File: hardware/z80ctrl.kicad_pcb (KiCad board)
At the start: 2 copper layers, 99.8 x 49.9 mm, 28 parts, among them J1 BUS, J2 BUSEXT, J4 IOADDR, J5 SERIAL1, J6 SERIAL2, J7 SD, SW1 RESET, SW2 HALT, U1 74HCT139, U2 ATMEGA1284P-PU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

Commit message: OCD tweaks
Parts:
- moved C3 0.25 mm to (239.3, 145.0)
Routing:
- net /SDCS: track 104.2 -> 102.1 mm

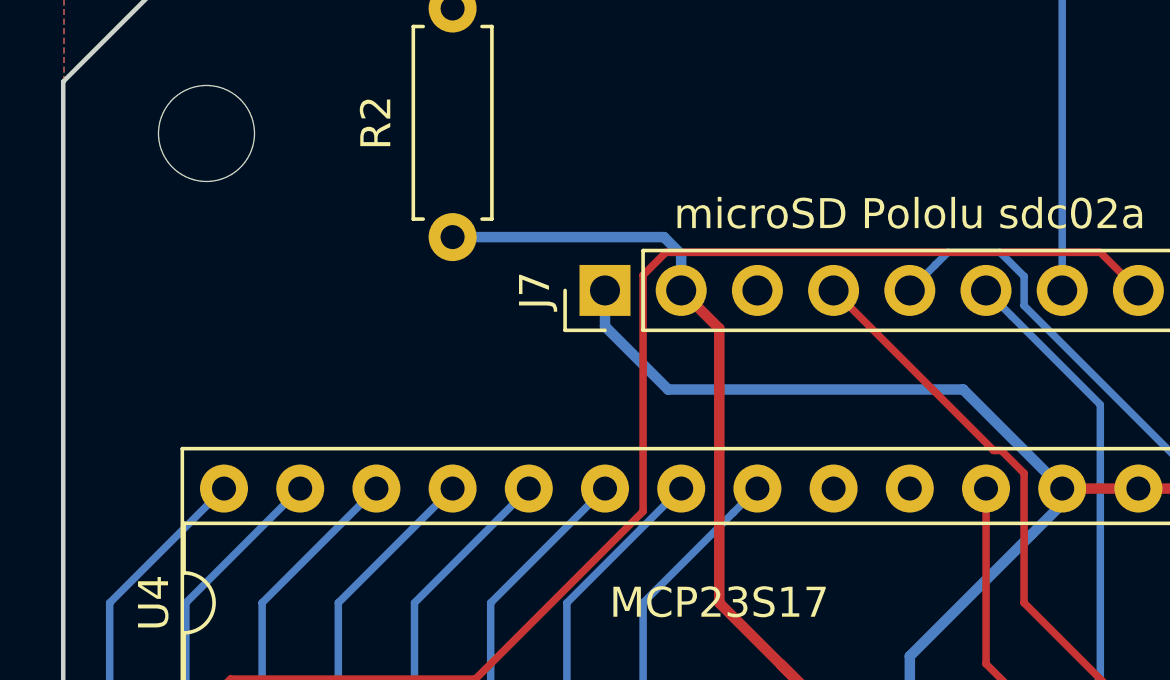
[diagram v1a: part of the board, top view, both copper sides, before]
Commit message: Add ISP header to REV2
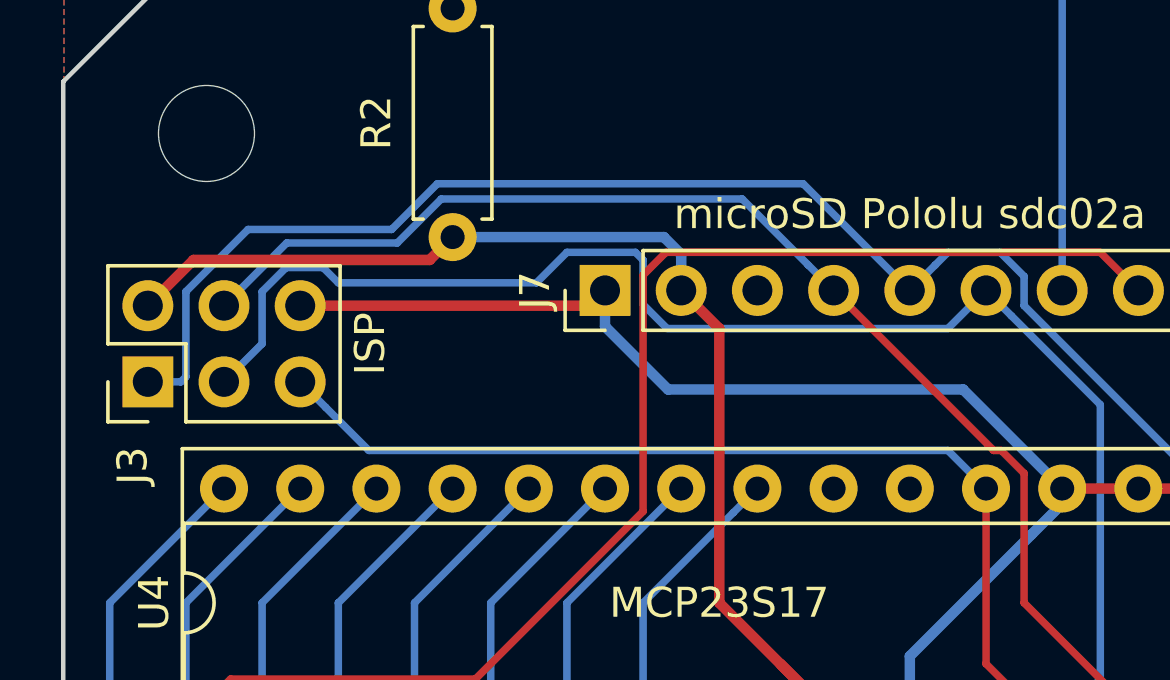
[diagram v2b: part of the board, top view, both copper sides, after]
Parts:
- added J3: ISP, Pin_Headers:Pin_Header_Straight_2x03_Pitch2.54mm, F.Cu at (157.0, 128.5)
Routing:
- net MISO: track 96.5 -> 127.8 mm
- net SCK: track 95.8 -> 126.9 mm
- net /AVRRST: track 129.7 -> 154.1 mm
- net MOSI: track 98.1 -> 121.1 mm
- net VCC: track 207.1 -> 218.2 mm
- net GND: track 308.0 -> 318.4 mm
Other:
- board text added: "z80ctrl REV2 (C)2018 J.B. Langston https://github.com/jblang/z80ctrl"
- board text removed: "(C)2018 J.B. Langston https://github.com/jblang/z80ctrl"
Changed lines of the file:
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@@
 (kicad_pcb (version 4) (host pcbnew 4.0.7)
   (general
-    (links 142)
+    (links 148)
     (no_connects 0)
-    (area 153.676999 46.9809 262.997001 153.663001)
+    (area 154.077599 103.429999 254.027601 153.440201)
     (thickness 1.6)
     (drawings 15)
-    (tracks 712)
+    (tracks 748)
     (zones 0)
-    (modules 28)
+    (modules 29)
     (nets 90)
   )
@@
     )
   )
+  (module Pin_Headers:Pin_Header_Straight_2x03_Pitch2.54mm (layer F.Cu)
+    (at 156.972 128.524 90)
+    (descr "Through hole straight pin header, 2x03, 2.54mm pitch, double rows")
+    (tags "Through hole pin header THT 2x03 2.54mm double row")
+    (fp_text reference J3 (at -2.794 -0.508 90) (layer F.SilkS)
+      (effects (font (size 1 1) (thickness 0.15)))
+    )
+    (fp_text value ISP (at 1.27 7.41 90) (layer F.SilkS)
+      (effects (font (size 1 1) (thickness 0.15)))
+    )
+    (fp_line (start 0 -1.27) (end 3.81 -1.27) (layer F.Fab) (width 0.1))
+    (fp_line (start 3.81 -1.27) (end 3.81 6.35) (layer F.Fab) (width 0.1))
+    (fp_line (start 3.81 6.35) (end -1.27 6.35) (layer F.Fab) (width 0.1))
+    (fp_line (start -1.27 6.35) (end -1.27 0) (layer F.Fab) (width 0.1))
+    (fp_line (start -1.27 0) (end 0 -1.27) (layer F.Fab) (width 0.1))
+    (fp_line (start -1.33 6.41) (end 3.87 6.41) (layer F.SilkS) (width 0.12))
+    (fp_line (start -1.33 1.27) (end -1.33 6.41) (layer F.SilkS) (width 0.12))
+    (fp_line (start 3.87 -1.33) (end 3.87 6.41) (layer F.SilkS) (width 0.12))
+    (fp_line (start -1.33 1.27) (end 1.27 1.27) (layer F.SilkS) (width 0.12))
+    (fp_line (start 1.27 1.27) (end 1.27 -1.33) (layer F.SilkS) (width 0.12))
+    (fp_line (start 1.27 -1.33) (end 3.87 -1.33) (layer F.SilkS) (width 0.12))
+    (fp_line (start -1.33 0) (end -1.33 -1.33) (layer F.SilkS) (width 0.12))
+    (fp_line (start -1.33 -1.33) (end 0 -1.33) (layer F.SilkS) (width 0.12))
+    (fp_line (start -1.8 -1.8) (end -1.8 6.85) (layer F.CrtYd) (width 0.05))
+    (fp_line (start -1.8 6.85) (end 4.35 6.85) (layer F.CrtYd) (width 0.05))
+    (fp_line (start 4.35 6.85) (end 4.35 -1.8) (layer F.CrtYd) (width 0.05))
+    (fp_line (start 4.35 -1.8) (end -1.8 -1.8) (layer F.CrtYd) (width 0.05))
+    (fp_text user %R (at 1.27 2.54 180) (layer F.Fab)
+      (effects (font (size 1 1) (thickness 0.15)))
+    )
+    (pad 1 thru_hole rect (at 0 0 90) (size 1.7 1.7) (drill 1) (layers *.Cu *.Mask)
+      (net 48 MISO))
+    (pad 2 thru_hole oval (at 2.54 0 90) (size 1.7 1.7) (drill 1) (layers *.Cu *.Mask)
+      (net 2 VCC))
+    (pad 3 thru_hole oval (at 0 2.54 90) (size 1.7 1.7) (drill 1) (layers *.Cu *.Mask)
+      (net 47 SCK))
+    (pad 4 thru_hole oval (at 2.54 2.54 90) (size 1.7 1.7) (drill 1) (layers *.Cu *.Mask)
+      (net 49 MOSI))
+    (pad 5 thru_hole oval (at 0 5.08 90) (size 1.7 1.7) (drill 1) (layers *.Cu *.Mask)
+      (net 43 /AVRRST))
+    (pad 6 thru_hole oval (at 2.54 5.08 90) (size 1.7 1.7) (drill 1) (layers *.Cu *.Mask)
+      (net 1 GND))
+    (model ${KISYS3DMOD}/Pin_Headers.3dshapes/Pin_Header_Straight_2x03_Pitch2.54mm.wrl
+      (at (xyz 0 0 0))
+      (scale (xyz 1 1 1))
+      (rotate (xyz 0 0 0))
+    )
+  )
   (gr_text "microSD Pololu sdc02a" (at 182.372 122.936) (layer F.SilkS)
     (effects (font (size 1 1) (thickness 0.15)))
@@
     (effects (font (size 1 1) (thickness 0.15)) (justify left mirror))
   )
-  (gr_text "(C)2018 J.B. Langston\nhttps://github.com/jblang/z80ctrl" (at 223.52 132.588) (layer B.SilkS)
+  (gr_text "z80ctrl REV2\n(C)2018 J.B. Langston\nhttps://github.com/jblang/z80ctrl" (at 223.52 132.08) (layer B.SilkS)
     (effects (font (size 1.5 1.5) (thickness 0.3)) (justify mirror))
   )
@@
   (gr_line (start 154.1526 118.5164) (end 154.1526 153.3652) (angle 90) (layer Edge.Cuts) (width 0.15))
   (gr_line (start 154.1526 153.3652) (end 253.9526 153.3652) (angle 90) (layer Edge.Cuts) (width 0.15))
+  (segment (start 162.052 125.984) (end 171.704 125.984) (width 0.35) (layer F.Cu) (net 1))
+  (segment (start 171.704 125.984) (end 172.212 125.476) (width 0.35) (layer F.Cu) (net 1))
   (segment (start 221.782 145.034) (end 223.56 146.812) (width 0.35) (layer F.Cu) (net 1))
   (segment (start 223.56 146.812) (end 239.99 146.812) (width 0.35) (layer F.Cu) (net 1))
@@
   (segment (start 224.282 142.24) (end 221.782 144.74) (width 0.35) (layer F.Cu) (net 1))
   (segment (start 221.782 144.74) (end 221.782 145.034) (width 0.35) (layer F.Cu) (net 1))
+  (segment (start 156.972 125.984) (end 158.496 124.46) (width 0.35) (layer F.Cu) (net 2))
+  (segment (start 166.37 124.46) (end 167.132 123.698) (width 0.35) (layer F.Cu) (net 2))
+  (segment (start 158.496 124.46) (end 166.37 124.46) (width 0.35) (layer F.Cu) (net 2))
   (segment (start 224.282 124.46) (end 225.806 122.936) (width 0.35) (layer F.Cu) (net 2))
   (segment (start 225.806 122.936) (end 227.33 122.936) (width 0.35) (layer F.Cu) (net 2))
@@
   (segment (start 228.6 145.034) (end 229.362 144.272) (width 0.25) (layer F.Cu) (net 42))
   (segment (start 229.362 142.24) (end 226.822 139.7) (width 0.25) (layer F.Cu) (net 42))
+  (segment (start 184.912 132.08) (end 183.642 130.81) (width 0.25) (layer B.Cu) (net 43))
+  (segment (start 183.642 130.81) (end 164.338 130.81) (width 0.25) (layer B.Cu) (net 43))
+  (segment (start 164.338 130.81) (end 162.901999 129.373999) (width 0.25) (layer B.Cu) (net 43))
+  (segment (start 162.901999 129.373999) (end 162.052 128.524) (width 0.25) (layer B.Cu) (net 43))
   (segment (start 242.062 109.982) (end 249.682 109.982) (width 0.25) (layer F.Cu) (net 43))
   (segment (start 249.682 109.982) (end 250.19 109.982) (width 0.25) (layer B.Cu) (net 43))
@@
   (segment (start 229.577002 109.474) (end 230.632 108.419002) (width 0.25) (layer B.Cu) (net 46))
   (segment (start 230.632 104.648) (end 230.124 104.14) (width 0.25) (layer B.Cu) (net 46))
+  (segment (start 159.512 128.524) (end 160.782 127.254) (width 0.25) (layer B.Cu) (net 47))
+  (segment (start 162.814 124.714) (end 163.322 125.222) (width 0.25) (layer B.Cu) (net 47))
+  (segment (start 163.322 125.222) (end 169.926 125.222) (width 0.25) (layer B.Cu) (net 47))
+  (segment (start 160.782 127.254) (end 160.782 125.514998) (width 0.25) (layer B.Cu) (net 47))
+  (segment (start 183.642 126.746) (end 184.912 125.476) (width 0.25) (layer B.Cu) (net 47))
+  (segment (start 160.782 125.514998) (end 161.582998 124.714) (width 0.25) (layer B.Cu) (net 47))
+  (segment (start 170.942 124.206) (end 173.227002 124.206) (width 0.25) (layer B.Cu) (net 47))
+  (segment (start 161.582998 124.714) (end 162.814 124.714) (width 0.25) (layer B.Cu) (net 47))
+  (segment (start 169.926 125.222) (end 170.942 124.206) (width 0.25) (layer B.Cu) (net 47))
+  (segment (start 173.227002 124.206) (end 173.482 124.460998) (width 0.25) (layer B.Cu) (net 47))
+  (segment (start 173.482 124.460998) (end 173.482 125.945002) (width 0.25) (layer B.Cu) (net 47))
+  (segment (start 173.482 125.945002) (end 174.282998 126.746) (width 0.25) (layer B.Cu) (net 47))
+  (segment (start 174.282998 126.746) (end 183.642 126.746) (width 0.25) (layer B.Cu) (net 47))
   (segment (start 247.991999 150.788001) (end 247.142 151.638) (width 0.25) (layer F.Cu) (net 47))
   (segment (start 248.412 150.368) (end 247.991999 150.788001) (width 0.25) (layer F.Cu) (net 47))
@@
   (segment (start 216.662 139.7) (end 213.925989 142.436011) (width 0.25) (layer F.Cu) (net 47))
   (segment (start 188.251999 140.499999) (end 187.452 139.7) (width 0.25) (layer F.Cu) (net 47))
+  (segment (start 160.312998 123.444) (end 158.242 125.514998) (width 0.25) (layer B.Cu) (net 48))
+  (segment (start 158.242 125.514998) (end 158.242 128.354) (width 0.25) (layer B.Cu) (net 48))
+  (segment (start 182.372 125.476) (end 178.816 121.92) (width 0.25) (layer B.Cu) (net 48))
+  (segment (start 178.816 121.92) (end 166.624 121.92) (width 0.25) (layer B.Cu) (net 48))
+  (segment (start 166.624 121.92) (end 165.1 123.444) (width 0.25) (layer B.Cu) (net 48))
+  (segment (start 165.1 123.444) (end 160.312998 123.444) (width 0.25) (layer B.Cu) (net 48))
+  (segment (start 158.242 128.354) (end 158.072 128.524) (width 0.25) (layer B.Cu) (net 48))
+  (segment (start 158.072 128.524) (end 156.972 128.524) (width 0.25) (layer B.Cu) (net 48))
   (segment (start 250.952 147.19441) (end 250.952 150.368) (width 0.25) (layer F.Cu) (net 48))
   (segment (start 217.227989 136.594011) (end 246.447601 136.594011) (width 0.25) (layer F.Cu) (net 48))
@@
   (segment (start 193.331999 140.499999) (end 192.532 139.7) (width 0.25) (layer F.Cu) (net 48))
   (segment (start 211.836 141.986) (end 194.818 141.986) (width 0.25) (layer F.Cu) (net 48))
+  (segment (start 178.982001 124.626001) (end 179.832 125.476) (width 0.25) (layer B.Cu) (net 49))
+  (segment (start 166.75241 122.428) (end 176.784 122.428) (width 0.25) (layer B.Cu) (net 49))
+  (segment (start 159.512 125.984) (end 161.601989 123.894011) (width 0.25) (layer B.Cu) (net 49))
+  (segment (start 165.2864 123.894011) (end 166.75241 122.428) (width 0.25) (layer B.Cu) (net 49))
+  (segment (start 176.784 122.428) (end 178.982001 124.626001) (width 0.25) (layer B.Cu) (net 49))
+  (segment (start 161.601989 123.894011) (end 165.2864 123.894011) (width 0.25) (layer B.Cu) (net 49))
   (segment (start 212.381999 138.900001) (end 211.582 139.7) (width 0.25) (layer F.Cu) (net 49))
   (segment (start 246.634 136.144) (end 215.138 136.144) (width 0.25) (layer F.Cu) (net 49))

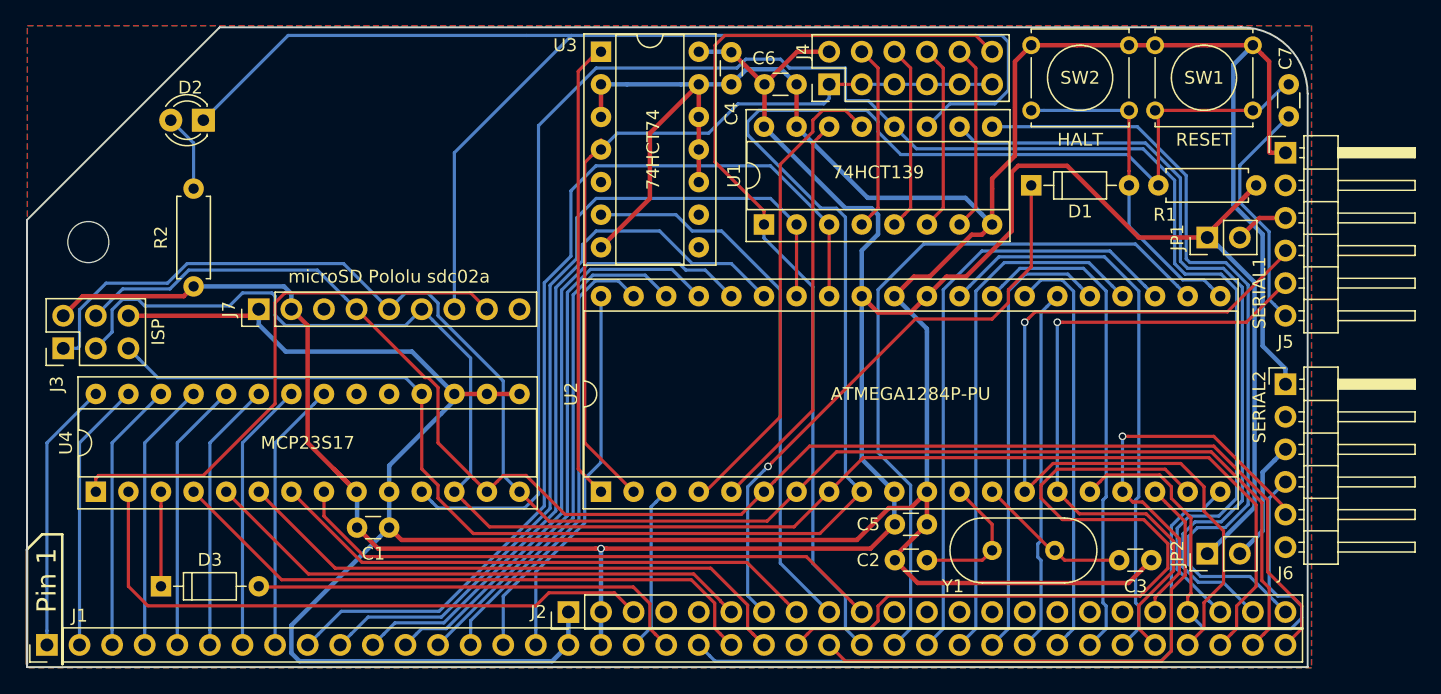
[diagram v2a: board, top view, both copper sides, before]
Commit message: REV3 board: Add Adafruit SD header; swap BUSRQ and M1; Replace RFSH with SD enable
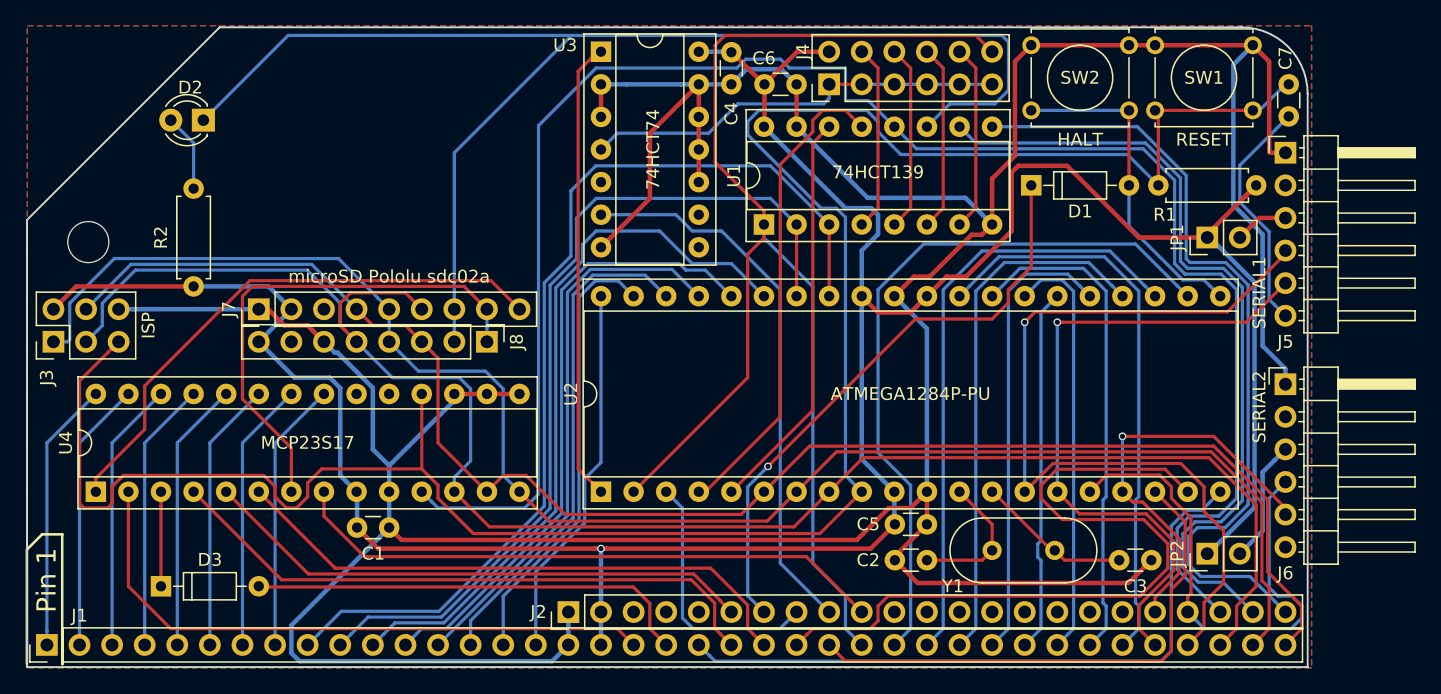
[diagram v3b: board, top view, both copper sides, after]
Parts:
- added J8: Adafruit SD, Pin_Headers:Pin_Header_Straight_1x08_Pitch2.54mm, F.Cu at (190.0, 128.0)
- J7: value SD -> Pololu SD
- R2: value 220 -> 1K
- moved J3 0.92 mm to (156.2, 128.0)
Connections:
- J7 pad 9: Net-(J7-Pad9) -> SDEN
- U2 pad 2: /IORQ2 -> /IORQ
- U2 pad 3: /M1 -> /BUSREQ
- U4 pad 1: /SDCD -> SDEN
- U4 pad 2: /RFSH -> /M1
- U4 pad 7: /BUSREQ -> /SDCD
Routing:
- net /RFSH: track 48.4 -> 0.00 mm
- net SDEN: track 0.00 -> 43.9 mm
- net /M1: track 13.0 -> 48.6 mm
- net /IORQ2: track 62.3 -> 33.2 mm
- net /IORQ: track 73.9 -> 98.9 mm
- net /BUSREQ: track 43.3 -> 20.1 mm
- net /AVRRST: track 154.1 -> 175.6 mm
- net SCK: track 126.9 -> 136.9 mm
- net /SDCD: track 43.2 -> 39.5 mm
- net /SDCS: track 102.1 -> 104.6 mm
- net MOSI: track 121.1 -> 123.4 mm
- net GND: track 318.4 -> 319.7 mm
- net VCC: track 218.2 -> 219.2 mm
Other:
- board text added: "z80ctrl REV3 (C)2018 J.B. Langston https://github.com/jblang/z80ctrl"
- board text removed: "z80ctrl REV2 (C)2018 J.B. Langston https://github.com/jblang/z80ctrl"

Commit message: More tweaks for REV3
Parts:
- removed JP2: Jumper, Pin_Headers:Pin_Header_Straight_1x02_Pitch2.54mm
- moved D1 64.9 mm to (175.5, 147.1)
- moved JP1 1.83 mm to (244.6, 120.9)
- moved SW1 0.51 mm to (242.1, 105.4)
- moved SW2 0.51 mm to (240.0, 110.5)
- moved R1 0.25 mm to (249.7, 115.8)
- moved C7 0.25 mm to (252.2, 110.5)
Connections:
- J4 pad 1: /IORQ2 -> VCC
- J4 pad 11: /IORQ2 -> /IORQ
- J4 pad 12: /IORQ -> Net-(J4-Pad10)
- J4 pad 2: VCC -> Net-(J4-Pad10)
- J4 pad 3: /IORQ2 -> Net-(J4-Pad3)
- J4 pad 4: Net-(J4-Pad4) -> Net-(J4-Pad10)
- J4 pad 5: /IORQ2 -> Net-(J4-Pad5)
- J4 pad 6: Net-(J4-Pad6) -> Net-(J4-Pad10)
- J4 pad 7: /IORQ2 -> Net-(J4-Pad7)
- J4 pad 8: Net-(J4-Pad8) -> Net-(J4-Pad10)
- J4 pad 9: /IORQ2 -> Net-(J4-Pad9)
- U1 pad 13: SPIA0 -> SPIA1
- U1 pad 14: SPIA1 -> SPIA0
- U1 pad 4: Net-(J4-Pad4) -> Net-(J4-Pad3)
- U1 pad 5: Net-(J4-Pad6) -> Net-(J4-Pad5)
- U1 pad 6: Net-(J4-Pad8) -> Net-(J4-Pad7)
- U1 pad 7: Net-(J4-Pad10) -> Net-(J4-Pad9)
- U2 pad 1: /IOACK -> /BUSREQ
- U2 pad 21: Net-(D1-Pad2) -> /BUSACK
- U2 pad 3: /BUSREQ -> /MREQ
- U3 pad 1: /IOACK -> /BUSREQ
- U3 pad 4: /IORQ2 -> Net-(J4-Pad10)
- U4 pad 2: /M1 -> /RFSH
- U4 pad 5: /BUSACK -> /M1
- U4 pad 6: /MREQ -> Net-(D1-Pad2)
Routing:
- net Net-(D1-Pad2): track 26.0 -> 128.2 mm
- net /RFSH: track 0.00 -> 44.3 mm
- net /BUSREQ: track 20.1 -> 61.9 mm
- net VCC: track 219.2 -> 181.7 mm
- net /IOACK: track 36.0 -> 0.00 mm
- net /IORQ2: track 33.2 -> 0.00 mm
- net /MREQ: track 45.4 -> 17.6 mm
- net /SDCS: track 104.6 -> 82.8 mm
- net Net-(J4-Pad10): track 14.5 -> 35.0 mm
- net /IOXCS: track 137.9 -> 121.1 mm
- net /BUSACK: track 43.3 -> 58.0 mm, vias 0 -> 1
- net Net-(J4-Pad6): track 14.5 -> 0.00 mm
- net Net-(J4-Pad4): track 14.5 -> 0.00 mm
- net Net-(J4-Pad8): track 14.5 -> 0.00 mm
- net Net-(J4-Pad9): track 0.00 -> 12.0 mm
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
